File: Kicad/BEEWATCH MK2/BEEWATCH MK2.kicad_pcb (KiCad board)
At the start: 4 copper layers, 83.4 x 40.3 mm, 120 parts, among them J1 USB_C_Receptacle_USB2.0_16P, J3 Conn_02x06_Odd_Even, J4 Conn_02x06_Odd_Even, Q1 DMG6968U, Q2 DMG6968U, Q3 DMP1045U-7, Q4 DMG6968U, Q5 BSS138, Q6 BSS138, Q7 BSS138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

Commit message: Antenna layout completed
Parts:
- moved TP1 1.80 mm to (160.9, 104.4)
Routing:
- net /RYS8830/GNSS_+1.8V: track 102.7 -> 107.6 mm, vias 7 -> 8
- net /ACCELEROMETER/MPU_SCL: track 20.7 -> 18.9 mm
- net /ACCELEROMETER/MPU_SDA: track 19.5 -> 18.2 mm
- net /ESP32/IO1: track 40.7 -> 39.8 mm
- net Net-(U1-CHIP_PU): track 11.2 -> 10.6 mm
- net GND: track 95.9 -> 96.5 mm

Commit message: Antenna layout completed
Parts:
- added TP2: TestPoint, TestPoint:TestPoint_Pad_D1.0mm, F.Cu at (159.7, 107.5)
- moved TP1 1.53 mm to (161.2, 105.9)
- moved L2 1.46 mm to (164.0, 110.3)
- moved C12 1.38 mm to (159.9, 110.3)
- moved C13 1.38 mm to (162.0, 109.8)
- moved AE1 0.50 mm to (167.7, 105.1)
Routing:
- net /RYS8830/GNSS_+1.8V: track 107.6 -> 100.2 mm
- net +3.3V: track 48.3 -> 45.0 mm
- net /ESP32/BUZZER_EN: track 23.3 -> 20.9 mm
- net /Display/TFT_D/C: track 16.7 -> 15.1 mm
- net GND: track 96.5 -> 95.0 mm, vias 81 -> 91
- net Net-(U1-LNA_IN): track 6.57 -> 5.21 mm
- net Net-(AE1-FEED): track 4.22 -> 5.23 mm
- net /Display/LED: track 25.4 -> 24.5 mm
- net /Display/TFT_SDI: track 20.1 -> 19.3 mm
- net /ESP32/IO1: track 39.8 -> 39.2 mm
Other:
- board text added: "RST"

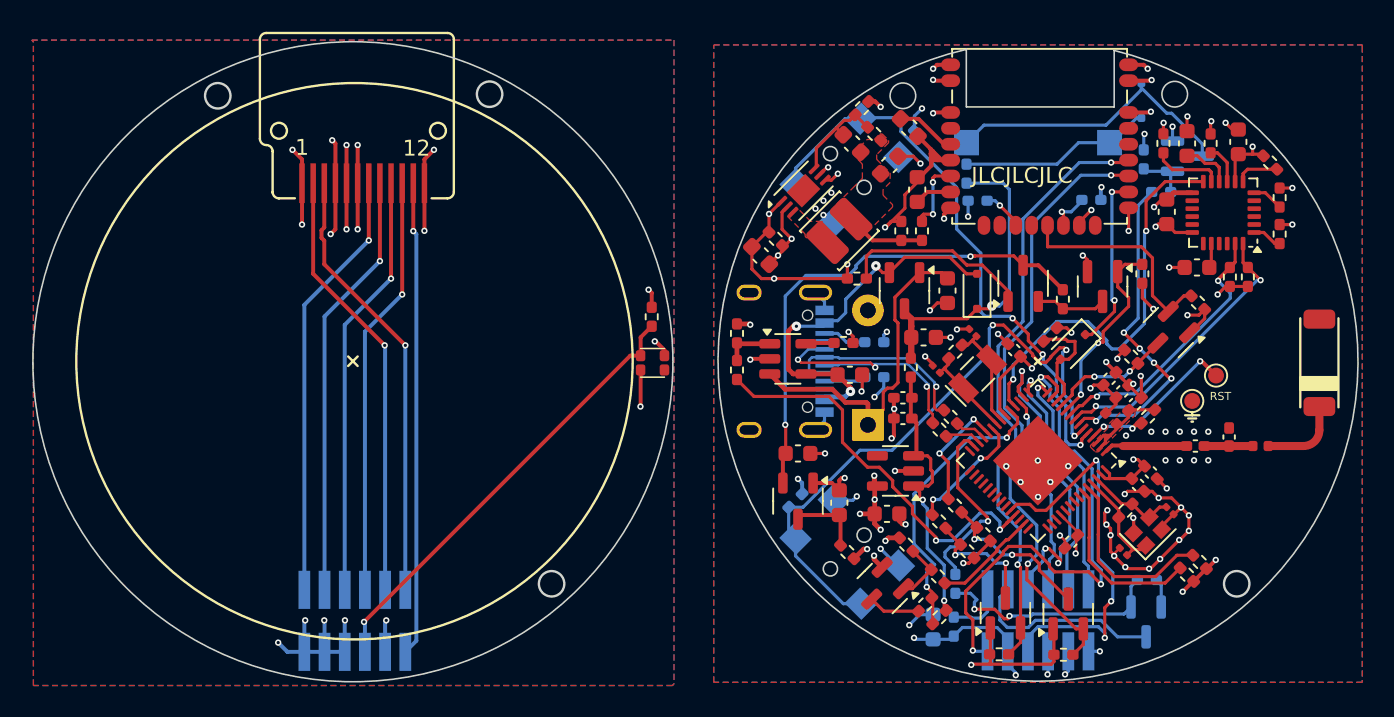
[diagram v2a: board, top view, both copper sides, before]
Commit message: Antenna and Schematic correction
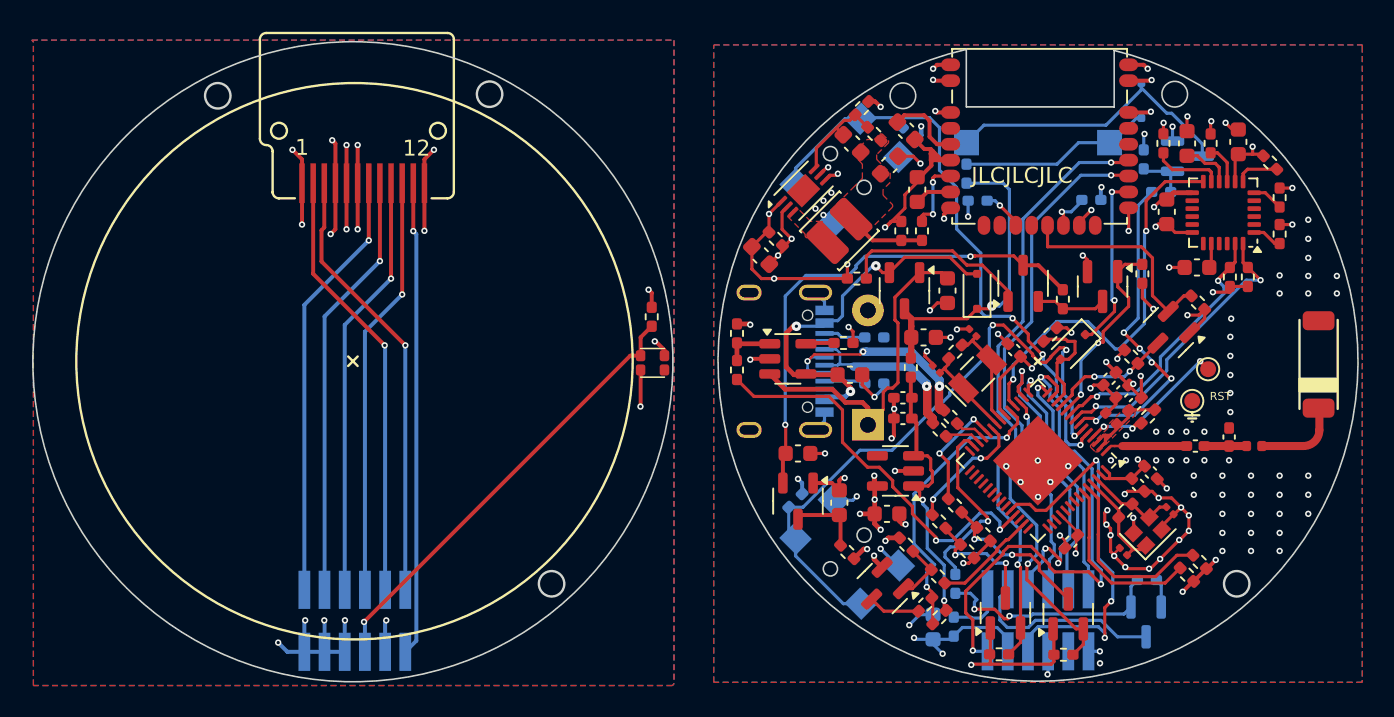
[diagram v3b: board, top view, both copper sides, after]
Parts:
- AE1: value Antenna_Chip -> CA-C03
- BT1: value Battery_Cell -> 3.7V 400mAh
- C12: value C_Small -> 0R
- C13: value C_Small -> 4.7nF
- C3, C4: value C_Small -> 12pF
- L1: value L_Small -> 2nH
- L2: value L -> 5.6nH
- L3: value L -> 3.3uH
- moved TP1 0.64 mm to (160.7, 105.5)
- moved R3 0.61 mm to (141.9, 90.7)
- moved L2 0.40 mm to (163.6, 110.3)
- moved R1 0.40 mm to (139.7, 106.4)
- moved R2 0.30 mm to (139.7, 103.5)
- moved C27 0.28 mm to (141.7, 90.5)
- moved meme_2 0.14 mm to (157.9, 105.4)
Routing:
- net /ESP32/D+: track 16.9 -> 11.5 mm, vias 3 -> 1
- net /ESP32/D-: track 12.7 -> 14.6 mm, vias 1 -> 3
- net GND: track 95.0 -> 93.3 mm, vias 91 -> 126
- net /ESP32/IO0: track 36.4 -> 38.1 mm
- net Net-(U7-LDO2_OUT): track 3.39 -> 4.87 mm
- net Net-(U1-CHIP_PU): track 10.7 -> 10.2 mm
- net /Display/TFT_LEDK: track 12.7 -> 12.1 mm

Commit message: Hope this by next week gerbers will generate
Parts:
- added mouse-bite-2.54mm-slot: VAL**, Panelization:mouse-bite-2.54mm-slot, F.Cu at (128.7, 105.0)
- U2: footprint Package_DFN_QFN:DFN-6-1EP_3x2mm_P0.5mm_EP1.65x1.35mm -> SM_BUCK:SON50P300X200X80-7N-D
- moved R6 0.57 mm to (126.3, 102.2)
- moved D1 0.24 mm to (126.0, 105.0)
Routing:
- net /Display board/_GND: track 33.6 -> 58.8 mm, vias 13 -> 12
- net /Display board/LED_K: track 27.5 -> 4.95 mm, vias 1 -> 2
- net /Display board/D/C: track 27.3 -> 5.30 mm, vias 1 -> 2
- net /Display board/3V3: track 10.5 -> 32.0 mm, vias 5 -> 4
- net /Display board/RST: track 29.8 -> 26.6 mm
- net /Display board/_LED: track 28.4 -> 29.4 mm
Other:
- board size 83.4 x 40.3 mm -> 82.7 x 40.3 mm
